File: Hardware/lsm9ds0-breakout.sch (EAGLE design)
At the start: 21 parts, among them U1 LSM9DS0

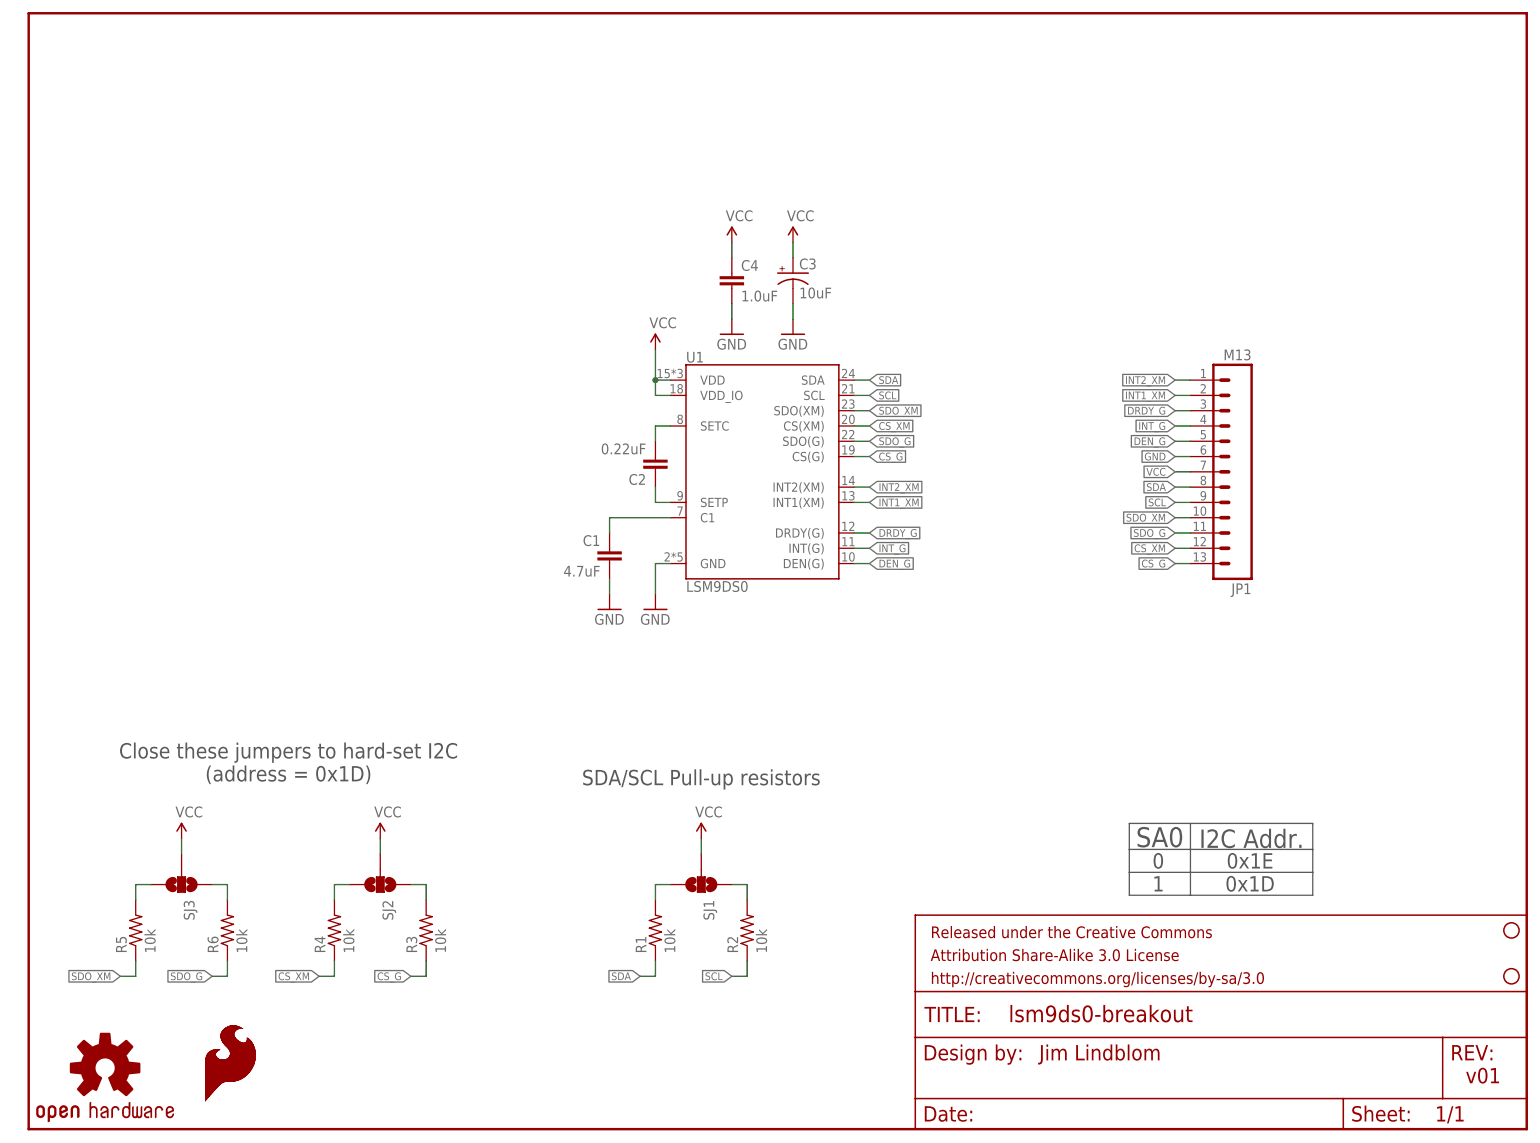
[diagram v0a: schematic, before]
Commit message: Fixed some silk. Moved some vias.
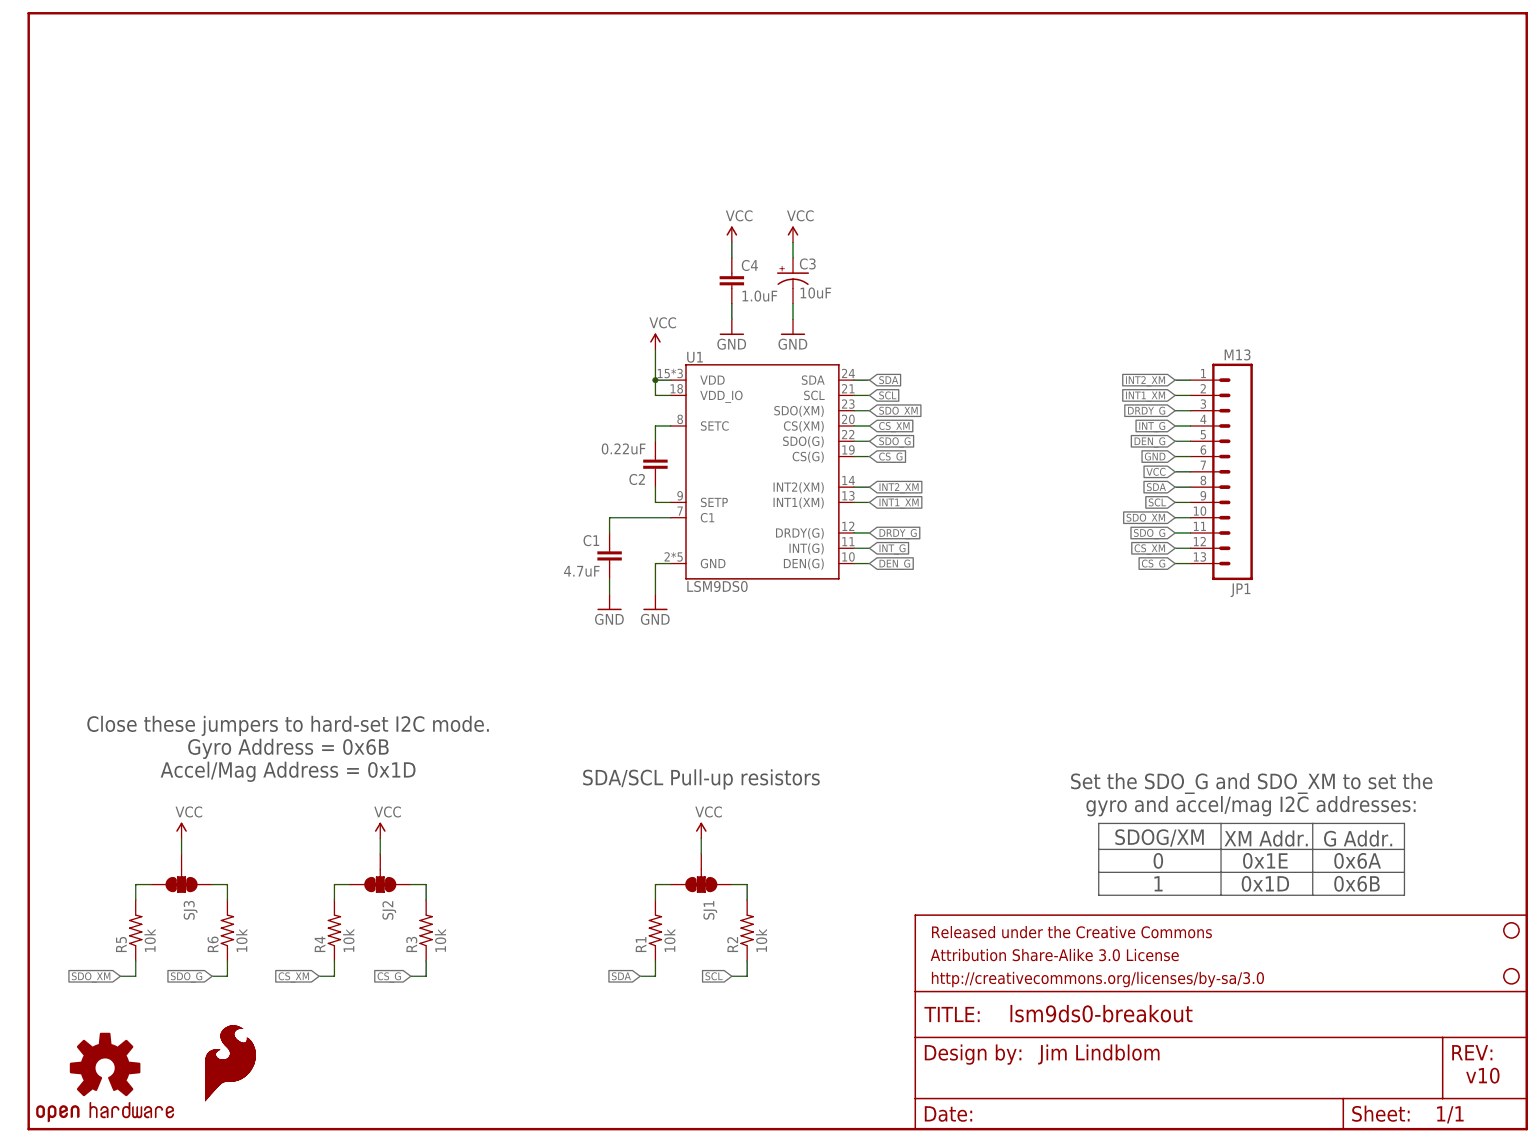
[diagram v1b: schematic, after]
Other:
- note added: "0x6A 0x6B"
- note added: "Close these jumpers to hard-set I2C mode. Gyro Address = 0x6B Accel/Mag Address = 0x1D"
- note added: "G Addr."
- note added: "SDOG/XM"
- note added: "Set the SDO_G and SDO_XM to set the gyro and accel/mag I2C addresses:"
- note added: "XM Addr."
- note added: "v10"
- note removed: "Close these jumpers to hard-set I2C (address = 0x1D)"
- note removed: "I2C Addr."
- note removed: "SA0"
- note removed: "v01"

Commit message: Adding fiducials
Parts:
- added FID1, FID2: FIDUCIALUFIDUCIAL, SparkFun-Aesthetics:FIDUCIALUFIDUCIAL
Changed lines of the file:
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@@
 <grid distance="0.1" unitdist="inch" unit="inch" style="lines" multiple="1" display="no" altdistance="0.01" altunitdist="inch" altunit="inch"/>
 <layers>
-<layer number="1" name="Top" color="4" fill="1" visible="yes" active="no"/>
-<layer number="2" name="Route2" color="1" fill="3" visible="yes" active="no"/>
-<layer number="3" name="Route3" color="4" fill="3" visible="yes" active="no"/>
-<layer number="4" name="Route4" color="1" fill="4" visible="yes" active="no"/>
-<layer number="5" name="Route5" color="4" fill="4" visible="yes" active="no"/>
-<layer number="6" name="Route6" color="1" fill="8" visible="yes" active="no"/>
-<layer number="7" name="Route7" color="4" fill="8" visible="yes" active="no"/>
-<layer number="8" name="Route8" color="1" fill="2" visible="yes" active="no"/>
-<layer number="9" name="Route9" color="4" fill="2" visible="yes" active="no"/>
-<layer number="10" name="Route10" color="1" fill="7" visible="yes" active="no"/>
-<layer number="11" name="Route11" color="4" fill="7" visible="yes" active="no"/>
-<layer number="12" name="Route12" color="1" fill="5" visible="yes" active="no"/>
-<layer number="13" name="Route13" color="4" fill="5" visible="yes" active="no"/>
-<layer number="14" name="Route14" color="1" fill="6" visible="yes" active="no"/>
-<layer number="15" name="Route15" color="4" fill="6" visible="yes" active="no"/>
-<layer number="16" name="Bottom" color="1" fill="1" visible="yes" active="no"/>
-<layer number="17" name="Pads" color="2" fill="1" visible="yes" active="no"/>
-<layer number="18" name="Vias" color="2" fill="1" visible="yes" active="no"/>
-<layer number="19" name="Unrouted" color="6" fill="1" visible="yes" active="no"/>
-<layer number="20" name="Dimension" color="15" fill="1" visible="yes" active="no"/>
-<layer number="21" name="tPlace" color="16" fill="1" visible="yes" active="no"/>
-<layer number="22" name="bPlace" color="14" fill="1" visible="yes" active="no"/>
-<layer number="23" name="tOrigins" color="15" fill="1" visible="yes" active="no"/>
-<layer number="24" name="bOrigins" color="15" fill="1" visible="yes" active="no"/>
-<layer number="25" name="tNames" color="7" fill="1" visible="yes" active="no"/>
-<layer number="26" name="bNames" color="7" fill="1" visible="yes" active="no"/>
-<layer number="27" name="tValues" color="7" fill="1" visible="yes" active="no"/>
-<layer number="28" name="bValues" color="7" fill="1" visible="yes" active="no"/>
+<layer number="1" name="Top" color="4" fill="1" visible="no" active="no"/>
+<layer number="2" name="Route2" color="1" fill="3" visible="no" active="no"/>
+<layer number="3" name="Route3" color="4" fill="3" visible="no" active="no"/>
+<layer number="4" name="Route4" color="1" fill="4" visible="no" active="no"/>
+<layer number="5" name="Route5" color="4" fill="4" visible="no" active="no"/>
+<layer number="6" name="Route6" color="1" fill="8" visible="no" active="no"/>
+<layer number="7" name="Route7" color="4" fill="8" visible="no" active="no"/>
+<layer number="8" name="Route8" color="1" fill="2" visible="no" active="no"/>
+<layer number="9" name="Route9" color="4" fill="2" visible="no" active="no"/>
+<layer number="10" name="Route10" color="1" fill="7" visible="no" active="no"/>
+<layer number="11" name="Route11" color="4" fill="7" visible="no" active="no"/>
+<layer number="12" name="Route12" color="1" fill="5" visible="no" active="no"/>
+<layer number="13" name="Route13" color="4" fill="5" visible="no" active="no"/>
+<layer number="14" name="Route14" color="1" fill="6" visible="no" active="no"/>
+<layer number="15" name="Route15" color="4" fill="6" visible="no" active="no"/>
+<layer number="16" name="Bottom" color="1" fill="1" visible="no" active="no"/>
+<layer number="17" name="Pads" color="2" fill="1" visible="no" active="no"/>
+<layer number="18" name="Vias" color="2" fill="1" visible="no" active="no"/>
+<layer number="19" name="Unrouted" color="6" fill="1" visible="no" active="no"/>
+<layer number="20" name="Dimension" color="15" fill="1" visible="no" active="no"/>
+<layer number="21" name="tPlace" color="16" fill="1" visible="no" active="no"/>
+<layer number="22" name="bPlace" color="14" fill="1" visible="no" active="no"/>
+<layer number="23" name="tOrigins" color="15" fill="1" visible="no" active="no"/>
+<layer number="24" name="bOrigins" color="15" fill="1" visible="no" active="no"/>
+<layer number="25" name="tNames" color="7" fill="1" visible="no" active="no"/>
+<layer number="26" name="bNames" color="7" fill="1" visible="no" active="no"/>
+<layer number="27" name="tValues" color="7" fill="1" visible="no" active="no"/>
+<layer number="28" name="bValues" color="7" fill="1" visible="no" active="no"/>
 <layer number="29" name="tStop" color="7" fill="3" visible="no" active="no"/>
 <layer number="30" name="bStop" color="7" fill="6" visible="no" active="no"/>
@@
 <layer number="35" name="tGlue" color="7" fill="4" visible="no" active="no"/>
 <layer number="36" name="bGlue" color="7" fill="5" visible="no" active="no"/>
-<layer number="37" name="tTest" color="7" fill="1" visible="yes" active="no"/>
-<layer number="38" name="bTest" color="7" fill="1" visible="yes" active="no"/>
+<layer number="37" name="tTest" color="7" fill="1" visible="no" active="no"/>
+<layer number="38" name="bTest" color="7" fill="1" visible="no" active="no"/>
 <layer number="39" name="tKeepout" color="4" fill="11" visible="no" active="no"/>
 <layer number="40" name="bKeepout" color="1" fill="11" visible="no" active="no"/>
@@
 <layer number="44" name="Drills" color="7" fill="1" visible="no" active="no"/>
 <layer number="45" name="Holes" color="7" fill="1" visible="no" active="no"/>
-<layer number="46" name="Milling" color="3" fill="1" visible="yes" active="no"/>
-<layer number="47" name="Measures" color="7" fill="1" visible="yes" active="no"/>
-<layer number="48" name="Document" color="7" fill="1" visible="yes" active="no"/>
-<layer number="49" name="Reference" color="7" fill="1" visible="yes" active="no"/>
-<layer number="50" name="dxf" color="7" fill="1" visible="yes" active="no"/>
-<layer number="51" name="tDocu" color="6" fill="1" visible="yes" active="no"/>
-<layer number="52" name="bDocu" color="7" fill="1" visible="yes" active="no"/>
-<layer number="53" name="tGND_GNDA" color="7" fill="9" visible="yes" active="no"/>
-<layer number="54" name="bGND_GNDA" color="1" fill="9" visible="yes" active="no"/>
-<layer number="56" name="wert" color="7" fill="1" visible="yes" active="no"/>
+<layer number="46" name="Milling" color="3" fill="1" visible="no" active="no"/>
+<layer number="47" name="Measures" color="7" fill="1" visible="no" active="no"/>
+<layer number="48" name="Document" color="7" fill="1" visible="no" active="no"/>
+<layer number="49" name="Reference" color="7" fill="1" visible="no" active="no"/>
+<layer number="50" name="dxf" color="7" fill="1" visible="no" active="no"/>
+<layer number="51" name="tDocu" color="6" fill="1" visible="no" active="no"/>
+<layer number="52" name="bDocu" color="7" fill="1" visible="no" active="no"/>
+<layer number="53" name="tGND_GNDA" color="7" fill="9" visible="no" active="no"/>
+<layer number="54" name="bGND_GNDA" color="1" fill="9" visible="no" active="no"/>
+<layer number="56" name="wert" color="7" fill="1" visible="no" active="no"/>
 <layer number="91" name="Nets" color="2" fill="1" visible="yes" active="yes"/>
 <layer number="92" name="Busses" color="1" fill="1" visible="yes" active="yes"/>
@@
 <part name="LOGO3" library="SparkFun-Aesthetics" deviceset="SFE_LOGO_FLAME" device=".1_INCH" value="SFE_LOGO_FLAME.1_INCH"/>
 <part name="LOGO2" library="SparkFun-Aesthetics" deviceset="SFE_LOGO_FLAME" device=".1_INCH" value="SFE_LOGO_FLAME.1_INCH"/>
+<part name="FID1" library="SparkFun-Aesthetics" deviceset="FIDUCIAL" device="UFIDUCIAL"/>
+<part name="FID2" library="SparkFun-Aesthetics" deviceset="FIDUCIAL" device="UFIDUCIAL"/>
 </parts>
 <sheets>
@@
 <instance part="LOGO3" gate="G$1" x="28.956" y="4.064"/>
 <instance part="LOGO2" gate="G$1" x="28.956" y="4.064"/>
+<instance part="FID1" gate="G$1" x="243.84" y="30.48"/>
+<instance part="FID2" gate="G$1" x="241.3" y="27.94"/>
 </instances>
 <busses>
